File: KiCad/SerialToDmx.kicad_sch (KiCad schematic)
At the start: 30 parts, among them Q1 2N3904, U1 XIAO ESP32 C3, U2 TEA1-0505, U3 H11L1, U4 H11L1, U5 H11L1, U6 ST485EBDR, U7 H11L1

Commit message: Started Work on Conn Box V2
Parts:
- removed DMXIN-J2, DMXOUT-J3, LED-J4: Conn_01x03_Socket, Connector_PinSocket_2.54mm:PinSocket_1x03_P2.54mm_Vertical, symbol Connector:Conn_01x03_Socket
- removed H1, H2, H3, H4: MountingHole_Pad, MountingHole:MountingHole_3.2mm_M3_Pad_TopBottom, symbol Mechanical:MountingHole_Pad
- removed PWR-J1: Conn_01x02_Socket, Connector_PinSocket_2.54mm:PinSocket_1x02_P2.54mm_Vertical, symbol Connector:Conn_01x02_Socket
- removed Q1: 2N3904, Package_TO_SOT_THT:TO-92_Inline, symbol Transistor_BJT:2N3904
- removed R10, R12, R5, R6: 330R, Resistor_THT:R_Axial_DIN0207_L6.3mm_D2.5mm_P10.16mm_Horizontal, symbol Device:R
- removed R11, R4, R7, R8, R9: 470R, Resistor_THT:R_Axial_DIN0207_L6.3mm_D2.5mm_P10.16mm_Horizontal, symbol Device:R
- removed U3, U4, U5, U7: H11L1, Package_DIP:DIP-6_W7.62mm_LongPads, symbol Isolator:H11L1
- removed U6: ST485EBDR, Package_SO:SO-8_5.3x6.2mm_P1.27mm, symbol Interface_UART:ST485EBDR
- added C1: 0.1uC, Capacitor_SMD:C_0402_1005Metric, symbol Device:C
- added J1: NAC3MPXXA, NeutrikCustom:NAC3MPXXA, symbol NeutrikCustom:NAC3MPXXA
- added J10, J11, J8, J9: Conn_01x08_Pin, Connector_Faston_Custom:Faston_01x08_pin, symbol Connector:Conn_01x08_Pin
- added J2: NAC3MPXXB, NeutrikCustom:NAC3MPXXB, symbol NeutrikCustom:NAC3MPXXB
- added J3: NC3FAV, NeutrikCustom:NC3FAV, symbol Connector_Audio:NC3FAV
- added J4: NC3MAV, NeutrikCustom:NC3MAV, symbol Connector_Audio:NC3MAV
- added J5: NC4FAV, NeutrikCustom:NC4FAV, symbol Connector_Audio:NC4FAV
- added J6, J7: Conn_01x08_Socket, Connector_Faston_Custom:Faston_01x08_socket, symbol Connector:Conn_01x08_Socket
- added PS1: IRM-45-12, IRM-45-12:CONV_IRM-45-12, symbol IRM-45-12:IRM-45-12
- added U2, U3, U4: ISOM8710DFFR, TICustom:ISOM8710, symbol ISOM8710:ISOM8710DFFR
- added U5: THVD1512DGS, TICustom:DGS0010A_N, symbol TICustom:THVD1512DGS
- added U6: SN74LV1T34DBV, Package_TO_SOT_SMD:SOT-23-5, symbol Logic_LevelTranslator:SN74LV1T34DBV
- D1: footprint Diode_THT:D_DO-41_SOD81_P10.16mm_Horizontal -> Diode_SMD:D_0402_1005Metric
- R1: value 120R -> 169R; footprint Resistor_THT:R_Axial_DIN0207_L6.3mm_D2.5mm_P10.16mm_Horizontal -> Resistor_SMD:R_0402_1005Metric
- R2: value 720R -> 169R; footprint Resistor_THT:R_Axial_DIN0207_L6.3mm_D2.5mm_P10.16mm_Horizontal -> Resistor_SMD:R_0402_1005Metric
- R3: value 720R -> 330R; footprint Resistor_THT:R_Axial_DIN0207_L6.3mm_D2.5mm_P10.16mm_Horizontal -> Resistor_SMD:R_0402_1005Metric
- renumbered PS1 to PS2, U2 to PS3
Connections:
- net 12V: now also J5.4, PS1.+V
- net 3V3: now also R1.1, U4.5 (VCC)
- net 5V: now also C1.2, U6.5 (VCC)
- net DMX_RX: now also U4.4 (OUT)
- net DMX_TX: now also U3.2 (CAT)
- net GND: now also C1.1, J1.G, J2.G, J4.G, J5.1, J5.2, J5.G, J6.4 (Pin_4), J7.4 (Pin_4), PS1.-V, U2.1 (AN), U4.3 (GND), U6.3 (GND)
- net GND_Iso: now also J3.1, J4.1, J6.1 (Pin_1), J7.1 (Pin_1), U2.3 (GND), U3.3 (GND), U5.2 (RE_N), U5.5 (GND); no longer R3.2
- net VCC_Iso: now also U2.5 (VCC), U3.5 (VCC), U4.1 (AN), U5.10 (VCC); no longer R2.1
- net at R2.2: now also U2.2 (CAT); no longer R1.2
- net at R3.1: now also U4.2 (CAT); no longer R1.1
- net DMX_READ renamed DMX_DRIVE
- net DMX_DRIVE: now also R2.1
- net LED_DATA renamed LED_DATA_33
- net LED_DATA_33: now also U6.2 (A)
- new net: U2.4 (OUT), U5.3 (DE)
- new net: R3.2, U5.1 (R)
- new net: R1.2, U3.1 (AN)
- new net: J10.1 (Pin_1), J11.1 (Pin_1)
- new net: J10.2 (Pin_2), J11.2 (Pin_2)
- new net: J10.3 (Pin_3), J11.3 (Pin_3)
- new net: U3.4 (OUT), U5.4 (D)
- new net DMX+: J3.3, J4.3, J6.3 (Pin_3), J7.3 (Pin_3), U5.6 (Y), U5.9 (A)
- new net DMX-: J3.2, J4.2, J6.2 (Pin_2), J7.2 (Pin_2), U5.7 (Z), U5.8 (B)
- new net GND-Connection-Bridge: J10.4 (Pin_4), J11.4 (Pin_4)
- new net GND-Connection-In-Termination: J8.4 (Pin_4)
- new net GND-Connection-Out-Termination: J9.4 (Pin_4)
- new net L: J6.7 (Pin_7), J7.7 (Pin_7), PS1.AC/L
- new net L-Connection-Bridge: J10.7 (Pin_7), J11.7 (Pin_7)
- new net L-Connection-Termination: J8.7 (Pin_7), J8.8 (Pin_8)
- new net L-switched: J1.L, J2.L, J6.8 (Pin_8)
- new net LED_DATA_50: J5.3, U6.4 (Y)
- new net N: J6.5 (Pin_5), J7.5 (Pin_5), PS1.AC/N
- new net N-Connection-Bridge: J10.5 (Pin_5), J11.5 (Pin_5)
- new net N-Connection-Termination: J8.5 (Pin_5), J8.6 (Pin_6)
- new net N-switched: J1.N, J2.N, J6.6 (Pin_6)
- no-connect marks 7 -> 23
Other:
- note added: "AC-In"
- note added: "AC-Out"
- note added: "Connectors"
- note added: "DMX Transceiver"
- note added: "DMX-In"
- note added: "DMX-Out"
- note added: "Daisy-Chain-Bridge"
- note added: "Daisy-Chain-In"
- note added: "Daisy-Chain-In-Termination"
- note added: "Daisy-Chain-Out"
- note added: "Daisy-Chain-Out-Termination"
- note added: "LED-Out"
- note added: "LED-Strip Level Shifter"
- note added: "MCU"
- note added: "Power"
- moved on the sheet: D1, PS2, PS3, U1

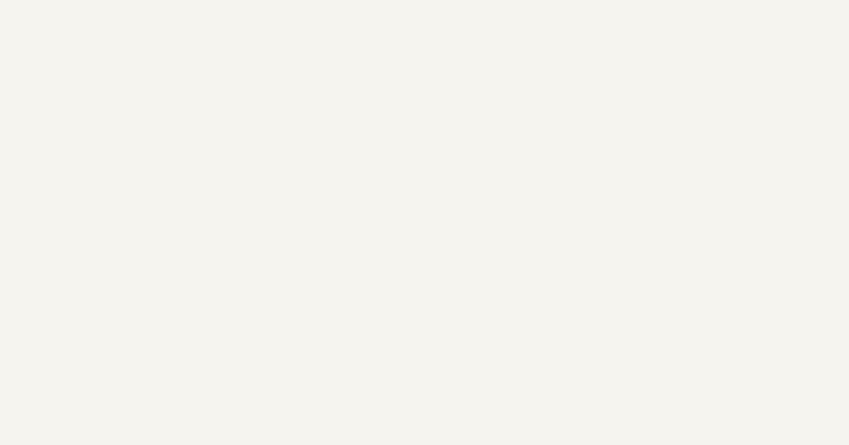
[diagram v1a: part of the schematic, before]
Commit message: Started on Mounting Holes for Terminators and Bridge
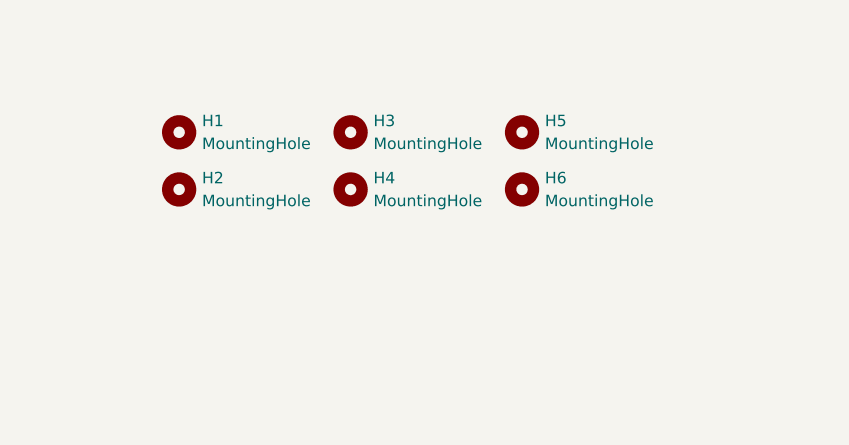
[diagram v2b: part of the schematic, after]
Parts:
- added H1, H2, H3, H4, H5, H6: MountingHole, MountingHole:MountingHole_3.2mm_M3, symbol Mechanical:MountingHole
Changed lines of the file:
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@@
+    )
+  )
+  (symbol (lib_id "Mechanical:MountingHole") (at 381 26.67 0) (unit 1)
+    (in_bom yes) (on_board yes) (dnp no) (fields_autoplaced)
+    (property "Reference" "H1" (at 383.54 25.4 0)
+      (effects (font (size 1.27 1.27)) (justify left))
+    )
+    (property "Value" "MountingHole" (at 383.54 27.94 0)
+      (effects (font (size 1.27 1.27)) (justify left))
+    )
+    (property "Footprint" "MountingHole:MountingHole_3.2mm_M3" (at 381 26.67 0)
+      (effects (font (size 1.27 1.27)) hide)
+    )
+    (property "Datasheet" "~" (at 381 26.67 0)
+      (effects (font (size 1.27 1.27)) hide)
+    )
+    (instances
+      (project "SerialToDmx"
+        (path "/cd59afbc-a244-4c38-a4e2-ea8e89e22dab"
+          (reference "H1") (unit 1)
+        )
+      )
     )
   )
@@
         (path "/cd59afbc-a244-4c38-a4e2-ea8e89e22dab"
           (reference "J2") (unit 1)
+        )
+      )
+    )
+  )
+  (symbol (lib_id "Mechanical:MountingHole") (at 400.05 26.67 0) (unit 1)
+    (in_bom yes) (on_board yes) (dnp no) (fields_autoplaced)
+    (property "Reference" "H3" (at 402.59 25.4 0)
+      (effects (font (size 1.27 1.27)) (justify left))
+    )
+    (property "Value" "MountingHole" (at 402.59 27.94 0)
+      (effects (font (size 1.27 1.27)) (justify left))
+    )
+    (property "Footprint" "MountingHole:MountingHole_3.2mm_M3" (at 400.05 26.67 0)
+      (effects (font (size 1.27 1.27)) hide)
+    )
+    (property "Datasheet" "~" (at 400.05 26.67 0)
+      (effects (font (size 1.27 1.27)) hide)
+    )
+    (instances
+      (project "SerialToDmx"
+        (path "/cd59afbc-a244-4c38-a4e2-ea8e89e22dab"
+          (reference "H3") (unit 1)
+        )
+      )
+    )
+  )
+  (symbol (lib_id "Mechanical:MountingHole") (at 400.05 33.02 0) (unit 1)
+    (in_bom yes) (on_board yes) (dnp no) (fields_autoplaced)
+    (property "Reference" "H4" (at 402.59 31.75 0)
+      (effects (font (size 1.27 1.27)) (justify left))
+    )
+    (property "Value" "MountingHole" (at 402.59 34.29 0)
+      (effects (font (size 1.27 1.27)) (justify left))
+    )
+    (property "Footprint" "MountingHole:MountingHole_3.2mm_M3" (at 400.05 33.02 0)
+      (effects (font (size 1.27 1.27)) hide)
+    )
+    (property "Datasheet" "~" (at 400.05 33.02 0)
+      (effects (font (size 1.27 1.27)) hide)
+    )
+    (instances
+      (project "SerialToDmx"
+        (path "/cd59afbc-a244-4c38-a4e2-ea8e89e22dab"
+          (reference "H4") (unit 1)
+        )
+      )
+    )
+  )
+  (symbol (lib_id "Mechanical:MountingHole") (at 381 33.02 0) (unit 1)
+    (in_bom yes) (on_board yes) (dnp no) (fields_autoplaced)
+    (property "Reference" "H2" (at 383.54 31.75 0)
+      (effects (font (size 1.27 1.27)) (justify left))
+    )
+    (property "Value" "MountingHole" (at 383.54 34.29 0)
+      (effects (font (size 1.27 1.27)) (justify left))
+    )
+    (property "Footprint" "MountingHole:MountingHole_3.2mm_M3" (at 381 33.02 0)
+      (effects (font (size 1.27 1.27)) hide)
+    )
+    (property "Datasheet" "~" (at 381 33.02 0)
+      (effects (font (size 1.27 1.27)) hide)
+    )
+    (instances
+      (project "SerialToDmx"
+        (path "/cd59afbc-a244-4c38-a4e2-ea8e89e22dab"
+          (reference "H2") (unit 1)
         )
       )
@@
         )
       )
+    )
+  )
+  (symbol (lib_id "Mechanical:MountingHole") (at 419.1 26.67 0) (unit 1)
+    (in_bom yes) (on_board yes) (dnp no) (fields_autoplaced)
+    (property "Reference" "H5" (at 421.64 25.4 0)
+      (effects (font (size 1.27 1.27)) (justify left))
+    )
+    (property "Value" "MountingHole" (at 421.64 27.94 0)
+      (effects (font (size 1.27 1.27)) (justify left))
+    )
+    (property "Footprint" "MountingHole:MountingHole_3.2mm_M3" (at 419.1 26.67 0)
+      (effects (font (size 1.27 1.27)) hide)
+    )
+    (property "Datasheet" "~" (at 419.1 26.67 0)
+      (effects (font (size 1.27 1.27)) hide)
+    )
+    (instances
+      (project "SerialToDmx"
+        (path "/cd59afbc-a244-4c38-a4e2-ea8e89e22dab"
+          (reference "H5") (unit 1)
+        )
+      )
+    )
+  )
+  (symbol (lib_id "Mechanical:MountingHole") (at 419.1 33.02 0) (unit 1)
+    (in_bom yes) (on_board yes) (dnp no) (fields_autoplaced)
+    (property "Reference" "H6" (at 421.64 31.75 0)
+      (effects (font (size 1.27 1.27)) (justify left))
+    )
+    (property "Value" "MountingHole" (at 421.64 34.29 0)
+      (effects (font (size 1.27 1.27)) (justify left))
+    )
+    (property "Footprint" "MountingHole:MountingHole_3.2mm_M3" (at 419.1 33.02 0)
+      (effects (font (size 1.27 1.27)) hide)
+    )
+    (property "Datasheet" "~" (at 419.1 33.02 0)
+      (effects (font (size 1.27 1.27)) hide)
+    )
+    (instances
+      (project "SerialToDmx"
+        (path "/cd59afbc-a244-4c38-a4e2-ea8e89e22dab"
+          (reference "H6") (unit 1)
+        )
+      )

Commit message: Improved Layout for Case
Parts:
- added H10, H11, H14, H7, H8, H9: Mousebite, Panelization:mouse-bite-2mm-slot, symbol Mechanical:MountingHole
- added H12, H13: Mousebite, Panelization:mouse-bite-3.5mm-slot, symbol Mechanical:MountingHole
- PS3: footprint Converter_DCDC:Converter_DCDC_TRACO_TEA1-xxxx_THT -> TracoCustom:CONV_TEA_1-0505
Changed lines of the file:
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@@
     (stroke (width 0) (type default))
   )
-  (polyline (pts (xy 430.53 120.65) (xy 430.53 210.82))
+  (polyline (pts (xy 430.53 120.65) (xy 430.53 228.6))
     (stroke (width 0) (type default))
   )
@@
     (stroke (width 0) (type default))
   )
-  (polyline (pts (xy 19.05 120.65) (xy 19.05 210.82))
+  (polyline (pts (xy 19.05 120.65) (xy 19.05 228.6))
     (stroke (width 0) (type default))
   )
@@
     (stroke (width 0) (type default))
   )
-  (polyline (pts (xy 430.53 210.82) (xy 19.05 210.82))
+  (polyline (pts (xy 430.53 228.6) (xy 19.05 228.6))
     (stroke (width 0) (type default))
   )
@@
         (path "/cd59afbc-a244-4c38-a4e2-ea8e89e22dab"
           (reference "H1") (unit 1)
+        )
+      )
+    )
+  )
+  (symbol (lib_id "Mechanical:MountingHole") (at 419.1 53.34 0) (unit 1)
+    (in_bom yes) (on_board yes) (dnp no) (fields_autoplaced)
+    (property "Reference" "H13" (at 421.64 52.07 0)
+      (effects (font (size 1.27 1.27)) (justify left))
+    )
+    (property "Value" "Mousebite" (at 421.64 54.61 0)
+      (effects (font (size 1.27 1.27)) (justify left))
+    )
+    (property "Footprint" "Panelization:mouse-bite-3.5mm-slot" (at 419.1 53.34 0)
+      (effects (font (size 1.27 1.27)) hide)
+    )
+    (property "Datasheet" "~" (at 419.1 53.34 0)
+      (effects (font (size 1.27 1.27)) hide)
+    )
+    (instances
+      (project "SerialToDmx"
+        (path "/cd59afbc-a244-4c38-a4e2-ea8e89e22dab"
+          (reference "H13") (unit 1)
         )
       )
@@
         (path "/cd59afbc-a244-4c38-a4e2-ea8e89e22dab"
           (reference "H3") (unit 1)
+        )
+      )
+    )
+  )
+  (symbol (lib_id "Mechanical:MountingHole") (at 381 46.99 0) (unit 1)
+    (in_bom yes) (on_board yes) (dnp no) (fields_autoplaced)
+    (property "Reference" "H7" (at 383.54 45.72 0)
+      (effects (font (size 1.27 1.27)) (justify left))
+    )
+    (property "Value" "Mousebite" (at 383.54 48.26 0)
+      (effects (font (size 1.27 1.27)) (justify left))
+    )
+    (property "Footprint" "Panelization:mouse-bite-2mm-slot" (at 381 46.99 0)
+      (effects (font (size 1.27 1.27)) hide)
+    )
+    (property "Datasheet" "~" (at 381 46.99 0)
+      (effects (font (size 1.27 1.27)) hide)
+    )
+    (instances
+      (project "SerialToDmx"
+        (path "/cd59afbc-a244-4c38-a4e2-ea8e89e22dab"
+          (reference "H7") (unit 1)
+        )
+      )
+    )
+  )
+  (symbol (lib_id "Mechanical:MountingHole") (at 438.15 46.99 0) (unit 1)
+    (in_bom yes) (on_board yes) (dnp no) (fields_autoplaced)
+    (property "Reference" "H10" (at 440.69 45.72 0)
+      (effects (font (size 1.27 1.27)) (justify left))
+    )
+    (property "Value" "Mousebite" (at 440.69 48.26 0)
+      (effects (font (size 1.27 1.27)) (justify left))
+    )
+    (property "Footprint" "Panelization:mouse-bite-2mm-slot" (at 438.15 46.99 0)
+      (effects (font (size 1.27 1.27)) hide)
+    )
+    (property "Datasheet" "~" (at 438.15 46.99 0)
+      (effects (font (size 1.27 1.27)) hide)
+    )
+    (instances
+      (project "SerialToDmx"
+        (path "/cd59afbc-a244-4c38-a4e2-ea8e89e22dab"
+          (reference "H10") (unit 1)
         )
       )
@@
     )
   )
+  (symbol (lib_id "Mechanical:MountingHole") (at 438.15 53.34 0) (unit 1)
+    (in_bom yes) (on_board yes) (dnp no) (fields_autoplaced)
+    (property "Reference" "H14" (at 440.69 52.07 0)
+      (effects (font (size 1.27 1.27)) (justify left))
+    )
+    (property "Value" "Mousebite" (at 440.69 54.61 0)
+      (effects (font (size 1.27 1.27)) (justify left))
+    )
+    (property "Footprint" "Panelization:mouse-bite-2mm-slot" (at 438.15 53.34 0)
+      (effects (font (size 1.27 1.27)) hide)
+    )
+    (property "Datasheet" "~" (at 438.15 53.34 0)
+      (effects (font (size 1.27 1.27)) hide)
+    )
+    (instances
+      (project "SerialToDmx"
+        (path "/cd59afbc-a244-4c38-a4e2-ea8e89e22dab"
+          (reference "H14") (unit 1)
+        )
+      )
+    )
+  )
+  (symbol (lib_id "Mechanical:MountingHole") (at 400.05 53.34 0) (unit 1)
+    (in_bom yes) (on_board yes) (dnp no) (fields_autoplaced)
+    (property "Reference" "H12" (at 402.59 52.07 0)
+      (effects (font (size 1.27 1.27)) (justify left))
+    )
+    (property "Value" "Mousebite" (at 402.59 54.61 0)
+      (effects (font (size 1.27 1.27)) (justify left))
+    )
+    (property "Footprint" "Panelization:mouse-bite-3.5mm-slot" (at 400.05 53.34 0)
+      (effects (font (size 1.27 1.27)) hide)
+    )
+    (property "Datasheet" "~" (at 400.05 53.34 0)
+      (effects (font (size 1.27 1.27)) hide)
+    )
+    (instances
+      (project "SerialToDmx"
+        (path "/cd59afbc-a244-4c38-a4e2-ea8e89e22dab"
+          (reference "H12") (unit 1)
+        )
+      )
+    )
+  )
   (symbol (lib_id "Connector:Conn_01x08_Socket") (at 337.82 165.1 270) (unit 1)
     (in_bom yes) (on_board yes) (dnp no)
@@
     )
   )
+  (symbol (lib_id "Mechanical:MountingHole") (at 381 53.34 0) (unit 1)
+    (in_bom yes) (on_board yes) (dnp no) (fields_autoplaced)
+    (property "Reference" "H11" (at 383.54 52.07 0)
+      (effects (font (size 1.27 1.27)) (justify left))
+    )
+    (property "Value" "Mousebite" (at 383.54 54.61 0)
+      (effects (font (size 1.27 1.27)) (justify left))
+    )
+    (property "Footprint" "Panelization:mouse-bite-2mm-slot" (at 381 53.34 0)
+      (effects (font (size 1.27 1.27)) hide)
+    )
+    (property "Datasheet" "~" (at 381 53.34 0)
+      (effects (font (size 1.27 1.27)) hide)
+    )
+    (instances
+      (project "SerialToDmx"
+        (path "/cd59afbc-a244-4c38-a4e2-ea8e89e22dab"
+          (reference "H11") (unit 1)
+        )
+      )
+    )
+  )
   (symbol (lib_id "Logic_LevelTranslator:SN74LV1T34DBV") (at 561.34 48.26 0) (unit 1)
     (in_bom yes) (on_board yes) (dnp no)
@@
         (path "/cd59afbc-a244-4c38-a4e2-ea8e89e22dab"
           (reference "J3") (unit 1)
+        )
+      )
+    )
+  )
+  (symbol (lib_id "Mechanical:MountingHole") (at 419.1 46.99 0) (unit 1)
+    (in_bom yes) (on_board yes) (dnp no) (fields_autoplaced)
+    (property "Reference" "H9" (at 421.64 45.72 0)
+      (effects (font (size 1.27 1.27)) (justify left))
+    )
+    (property "Value" "Mousebite" (at 421.64 48.26 0)
+      (effects (font (size 1.27 1.27)) (justify left))
+    )
+    (property "Footprint" "Panelization:mouse-bite-2mm-slot" (at 419.1 46.99 0)
+      (effects (font (size 1.27 1.27)) hide)
+    )
+    (property "Datasheet" "~" (at 419.1 46.99 0)
+      (effects (font (size 1.27 1.27)) hide)
+    )
+    (instances
+      (project "SerialToDmx"
+        (path "/cd59afbc-a244-4c38-a4e2-ea8e89e22dab"
+          (reference "H9") (unit 1)
         )
       )
@@
     )
   )
+  (symbol (lib_id "Mechanical:MountingHole") (at 400.05 46.99 0) (unit 1)
+    (in_bom yes) (on_board yes) (dnp no) (fields_autoplaced)
+    (property "Reference" "H8" (at 402.59 45.72 0)
+      (effects (font (size 1.27 1.27)) (justify left))
+    )
+    (property "Value" "Mousebite" (at 402.59 48.26 0)
+      (effects (font (size 1.27 1.27)) (justify left))
+    )
+    (property "Footprint" "Panelization:mouse-bite-2mm-slot" (at 400.05 46.99 0)
+      (effects (font (size 1.27 1.27)) hide)
+    )
+    (property "Datasheet" "~" (at 400.05 46.99 0)
+      (effects (font (size 1.27 1.27)) hide)
+    )
+    (instances
+      (project "SerialToDmx"
+        (path "/cd59afbc-a244-4c38-a4e2-ea8e89e22dab"
+          (reference "H8") (unit 1)
+        )
+      )
+    )
+  )
   (symbol (lib_id "R-78E5.0-0.5:R-78E5.0-0.5") (at 45.72 62.865 0) (unit 1)
     (in_bom yes) (on_board yes) (dnp no) (fields_autoplaced)
@@
       (effects (font (size 1.27 1.27)))
     )
-    (property "Footprint" "Converter_DCDC:Converter_DCDC_TRACO_TEA1-xxxx_THT" (at 45.72 90.805 0)
-      (effects (font (size 1.27 1.27)) hide)
-    )
+    (property "Footprint" "TracoCustom:CONV_TEA_1-0505" (at 45.72 90.805 0)
+      (effects (font (size 1.27 1.27)) hide)
+    )
